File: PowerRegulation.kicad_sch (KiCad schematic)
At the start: 68 parts, among them J1 Logic_Power_Switch, J2 XT60-M, J3 24V_Lockout_Key_Switch, K1 G5Q-1A DC24, Q1 BSS138, Q2 BSS138, Q3 DMP6023LE-13, U1 LM3880-1AA, U2 LMR33630BDDA, U3 TPS78533QKVURQ1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

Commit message: start pcb design
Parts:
- removed R28: 100k, Resistor_SMD:R_0603_1608Metric, symbol Device:R_Small_US
- removed U4: TLC555xD, Package_SO:SOIC-8_3.9x4.9mm_P1.27mm, symbol Timer:TLC555xD
- added U14: TLC555xPS, Package_SO:VSSOP-8_3x3mm_P0.65mm, symbol Timer:TLC555xPS
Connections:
- net +3.3V: now also R20.2
- net +5.3V: now also U14.8 (VCC)
- net GND: now also U14.1 (GND)
- net TR: now also U14.2 (TR), U14.6 (THR)
- net VCC: no longer R20.2
- net at BZ1.2 (-): now also U14.3 (Q)
- net at R23.1, R24.2: now also U14.4 (R)
- net at C11.2: now also U14.5 (CV)
- net at R26.1, R27.1: now also U14.7 (DIS)
- no-connect marks 0 -> 1
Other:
- moved on the sheet: C21

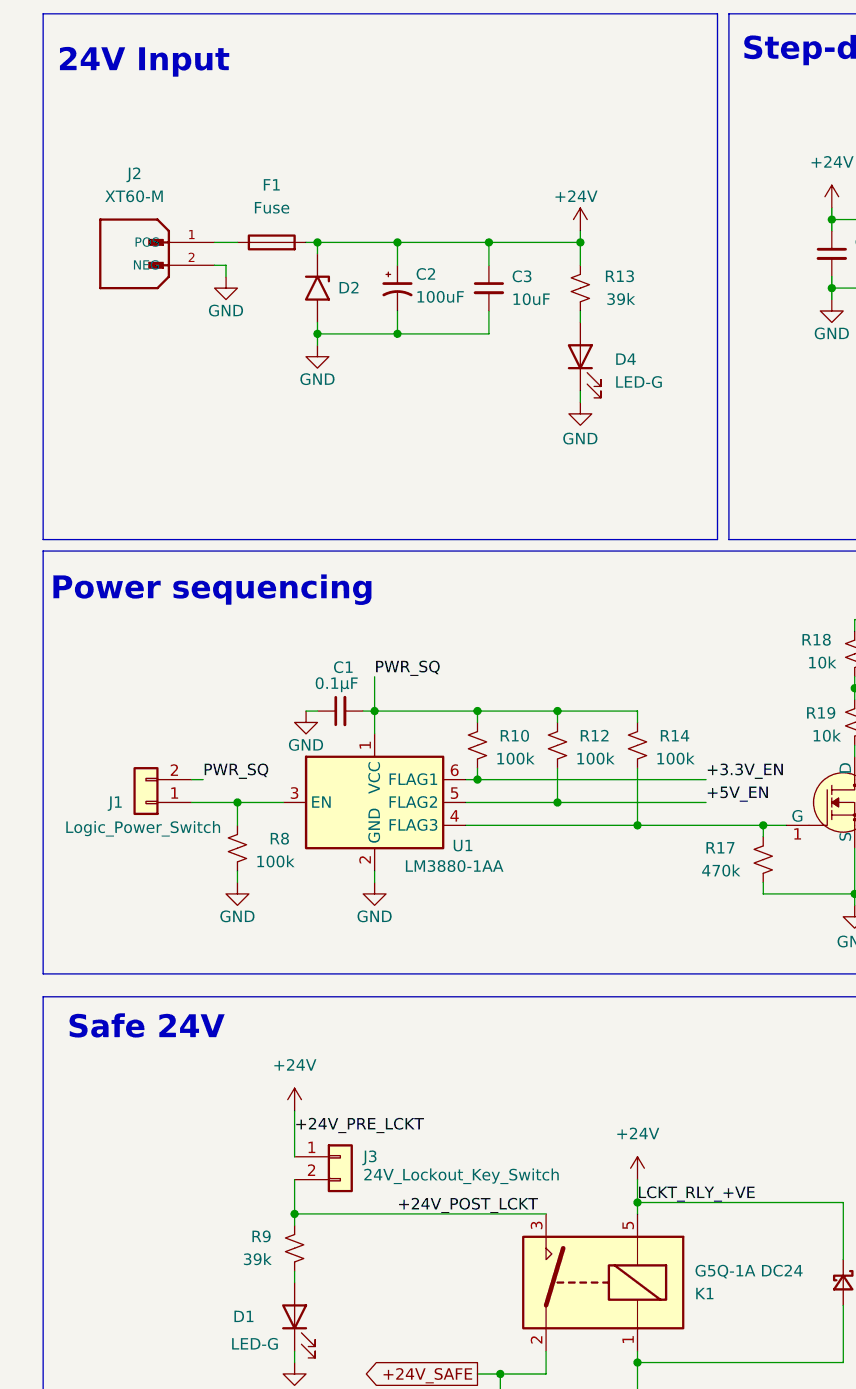
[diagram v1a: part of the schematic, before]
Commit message: change connectors and more progress on pcb
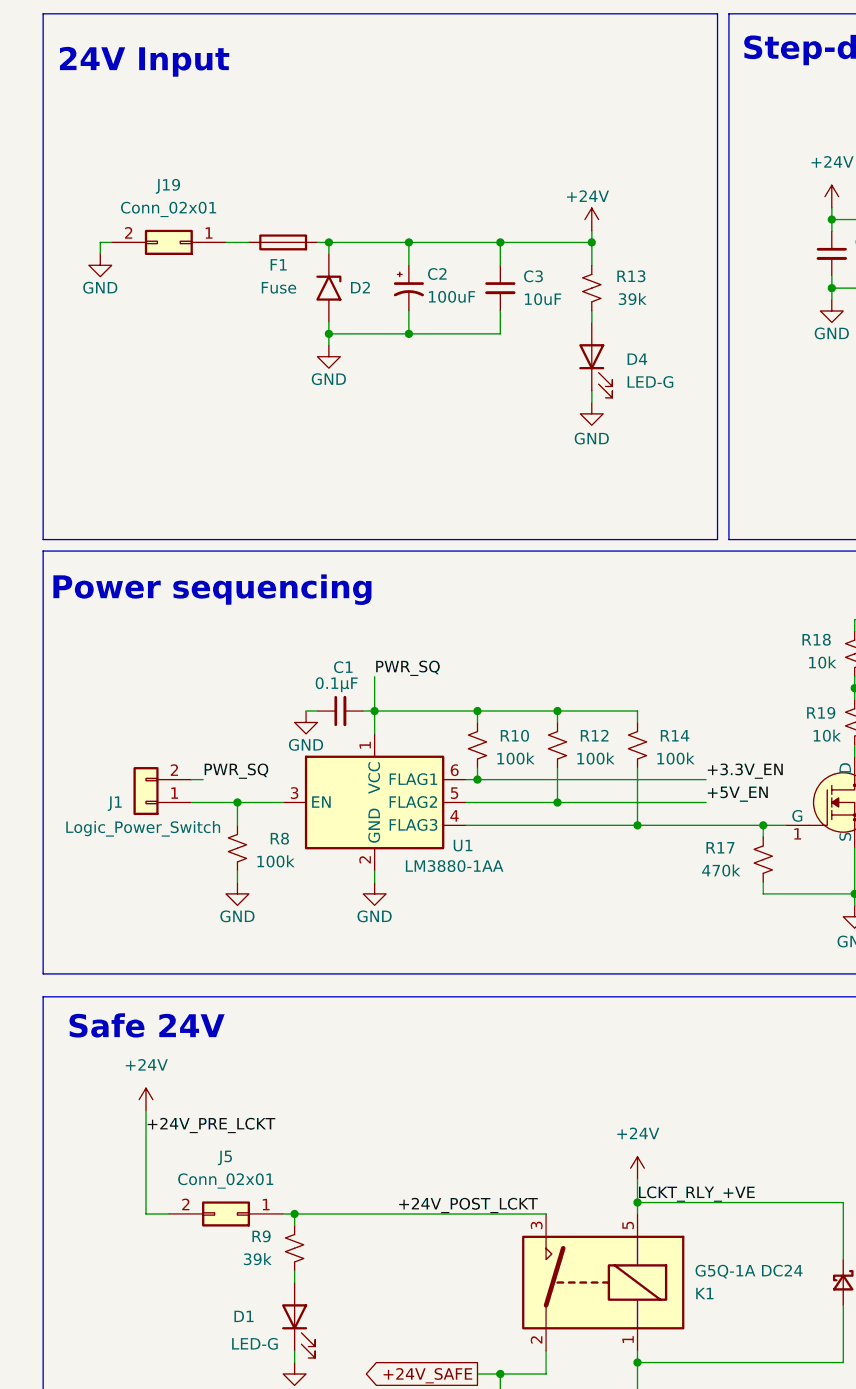
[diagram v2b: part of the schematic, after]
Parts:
- removed J2: XT60-M, Connector_AMASS:AMASS_XT60PW-F_1x02_P7.20mm_Horizontal, symbol XT60-M:XT60-M
- removed J3: 24V_Lockout_Key_Switch, Connector_JST:JST_XH_B2B-XH-A_1x02_P2.50mm_Vertical, symbol Connector_Generic:Conn_01x02
- added J19, J5: Conn_02x01, Connector_Molex:Molex_Mini-Fit_Jr_5566-02A_2x01_P4.20mm_Vertical, symbol Connector_Generic:Conn_02x01
- C3: footprint Capacitor_SMD:C_1206_3216Metric -> Capacitor_SMD:C_1812_4532Metric; LCSC C13585 -> (none)
- J1: footprint Connector_JST:JST_XH_B2B-XH-A_1x02_P2.50mm_Vertical -> Connector_Molex:Molex_KK-396_A-41791-0002_1x02_P3.96mm_Vertical
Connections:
- net +24V: now also J5.2 (Pin_2)
- net +24V_POST_LCKT: now also J5.1 (Pin_1)
- net GND: now also J19.2 (Pin_2)
- net at F1.1: now also J19.1 (Pin_1)
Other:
- moved on the sheet: C2, C3, D2, D4, F1, R13

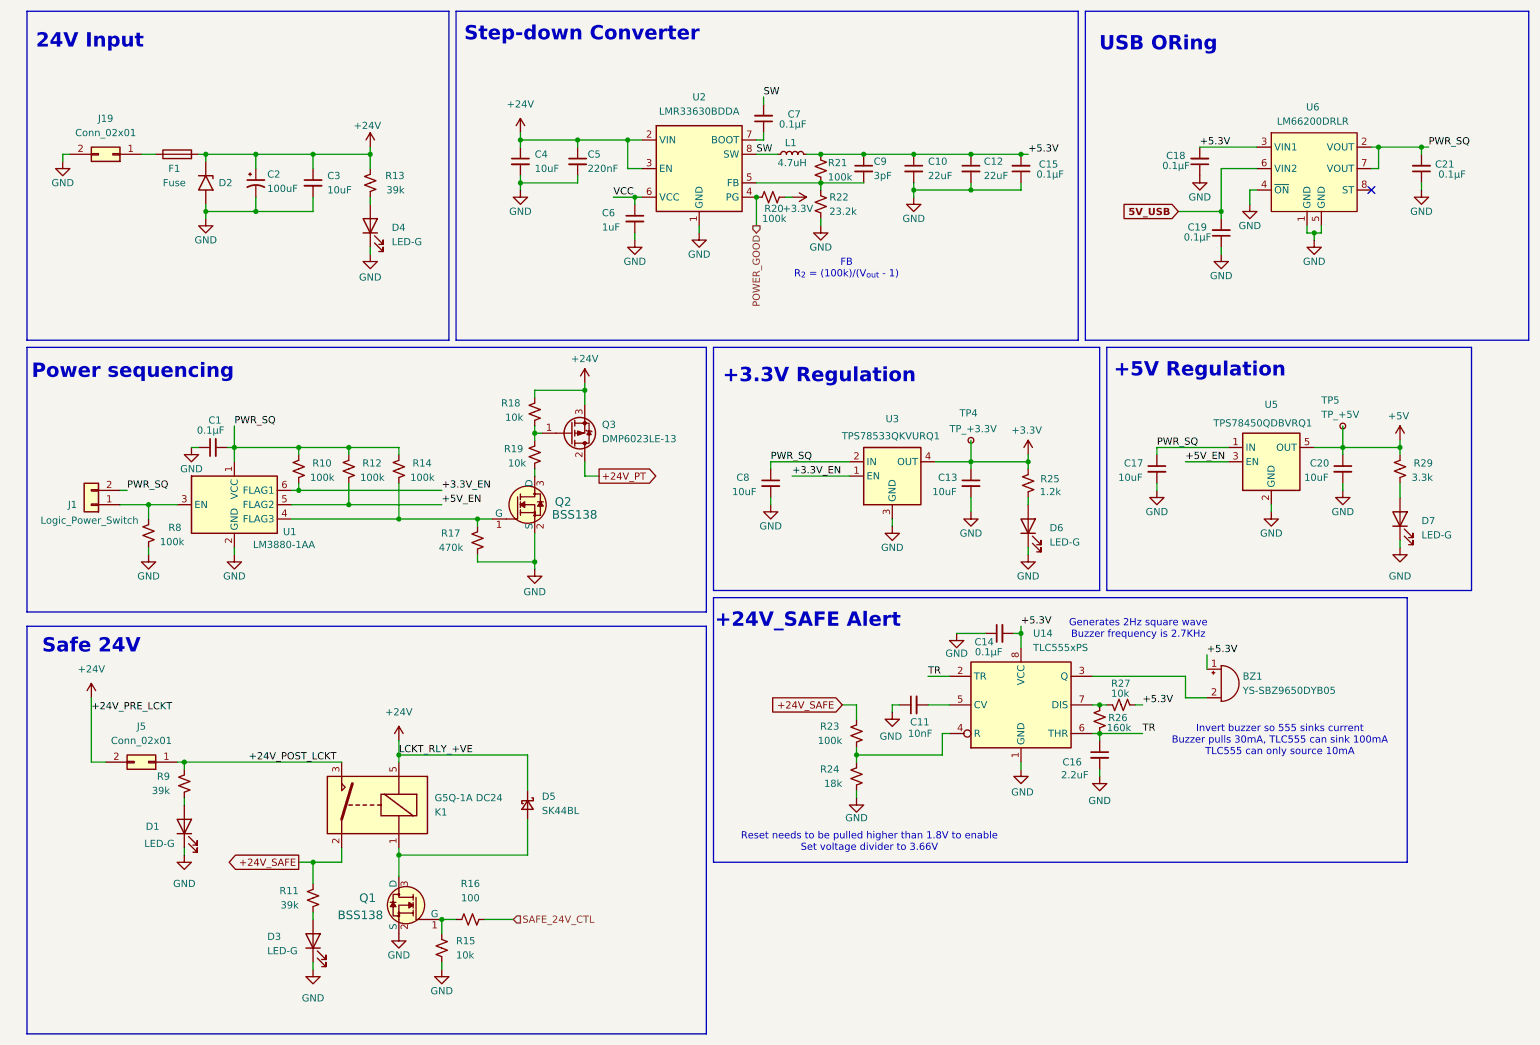
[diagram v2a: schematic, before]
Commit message: change clamping resistors on tc adcs for lower leakage current
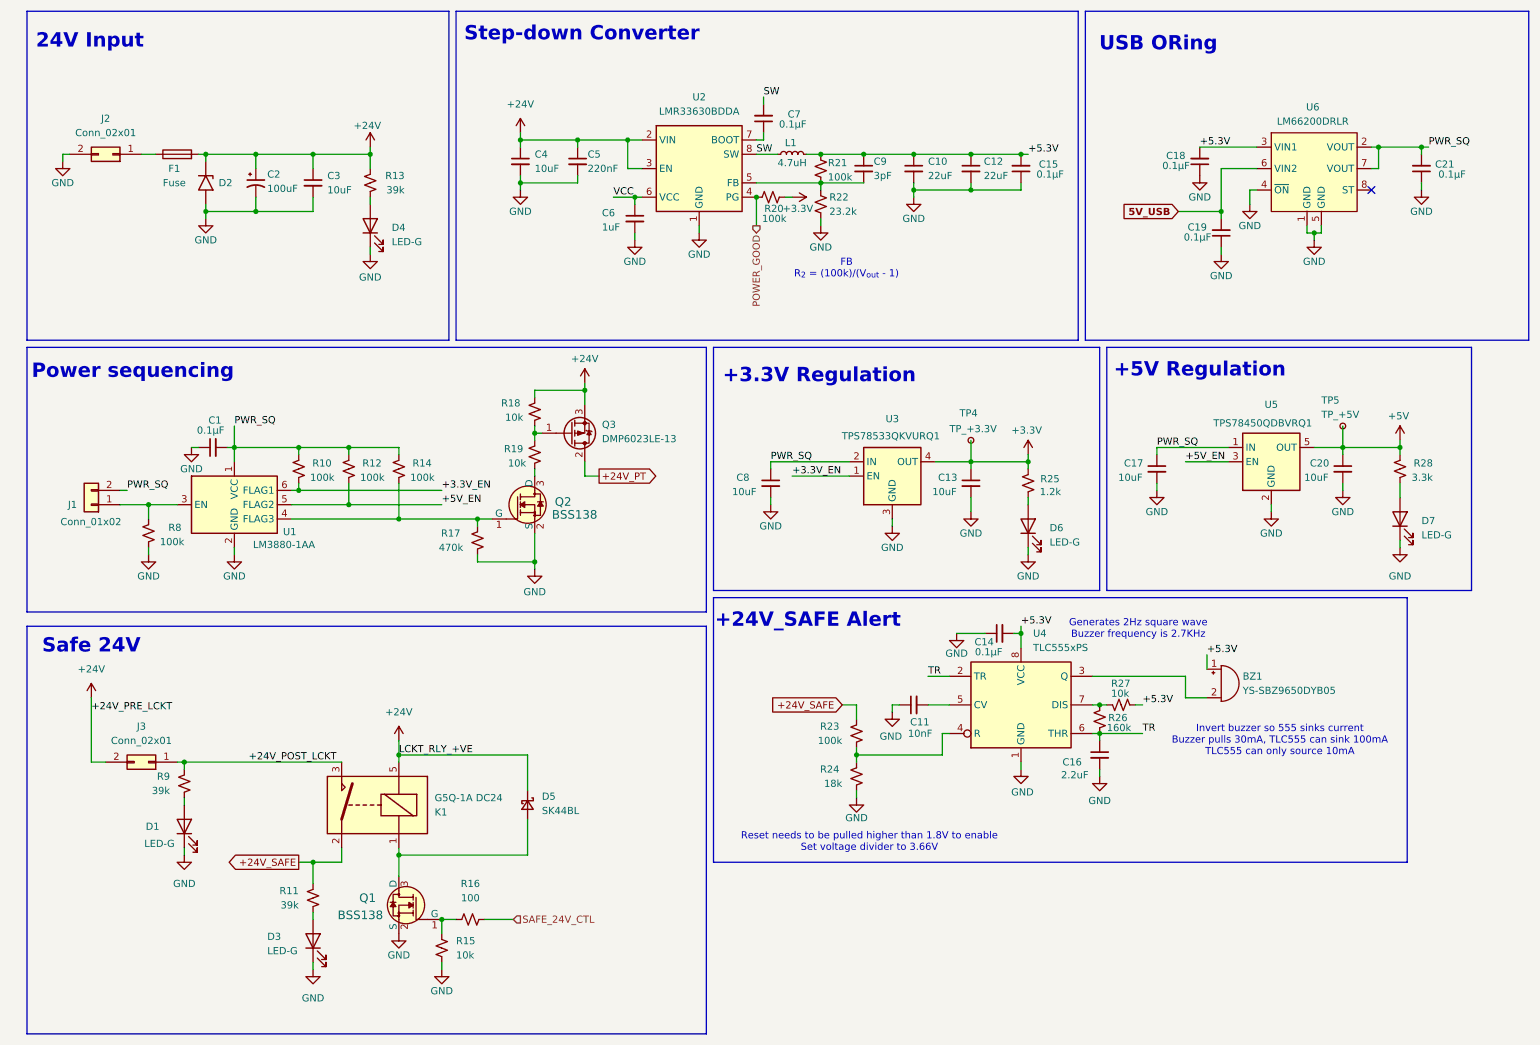
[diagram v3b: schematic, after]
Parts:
- BZ1: footprint (none) -> Library:YS-SBZ9650DYB05
- J1: value Logic_Power_Switch -> Conn_01x02; footprint Connector_Molex:Molex_KK-396_A-41791-0002_1x02_P3.96mm_Vertical -> Connector_Molex:Molex_Micro-Fit_3.0_43650-0215_1x02_P3.00mm_Vertical; LCSC C20079 -> (none); MPN XH-2A -> (none); now in the parts list
- renumbered J19 to J2, J5 to J3, R29 to R28, U14 to U4
